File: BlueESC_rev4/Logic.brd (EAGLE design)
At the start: 24.4 x 36 mm, 37 parts, among them U1 ATMEGA168, U2 V_REG_LDOSMD, Y1 RESONATORSMD

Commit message: Commit before major changes to rev 4
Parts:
- R15: value 22 -> 150
- R16: value 22 -> 100
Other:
- board text added: "BLUESC-ELEC-LOGIC-X1B"
- board text removed: "BLUESC-ELEC-LOGIC-X1A"
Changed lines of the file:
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@@
 <hole x="23.495" y="10.795" drill="2.8"/>
 <hole x="27.305" y="10.795" drill="2.8"/>
-<text x="31.115" y="43.02125" size="0.6096" layer="51" rot="R180">BLUESC-ELEC-LOGIC-X1A</text>
+<text x="31.115" y="43.02125" size="0.6096" layer="51" rot="R180">BLUESC-ELEC-LOGIC-X1B</text>
 <text x="23.495" y="20.6375" size="0.6096" layer="51" rot="R180">GND</text>
 <text x="25.0825" y="20.6375" size="0.6096" layer="51" rot="R180">5V</text>
@@
 <element name="R13" library="SparkFun-Resistors" package="0603-RES" value="10K" x="23.92375" y="14.57" rot="R270"/>
 <element name="R14" library="SparkFun-Resistors" package="0603-RES" value="10K" x="26.46375" y="14.605" rot="R270"/>
-<element name="R15" library="SparkFun" package="0603-RES" value="22" x="21.55" y="14.56" rot="R90"/>
-<element name="R16" library="SparkFun" package="0603-RES" value="22" x="28.94" y="14.5575" rot="R90"/>
+<element name="R15" library="SparkFun" package="0603-RES" value="150" x="21.55" y="14.56" rot="R90"/>
+<element name="R16" library="SparkFun" package="0603-RES" value="100" x="28.94" y="14.5575" rot="R90"/>
 <element name="R2" library="SparkFun-Resistors" package="0603-RES" value="47K" x="20.0025" y="26.19375" rot="R180"/>
 <element name="R3" library="SparkFun-Resistors" package="0603-RES" value="47K" x="19.52625" y="28.8925" rot="R90"/>

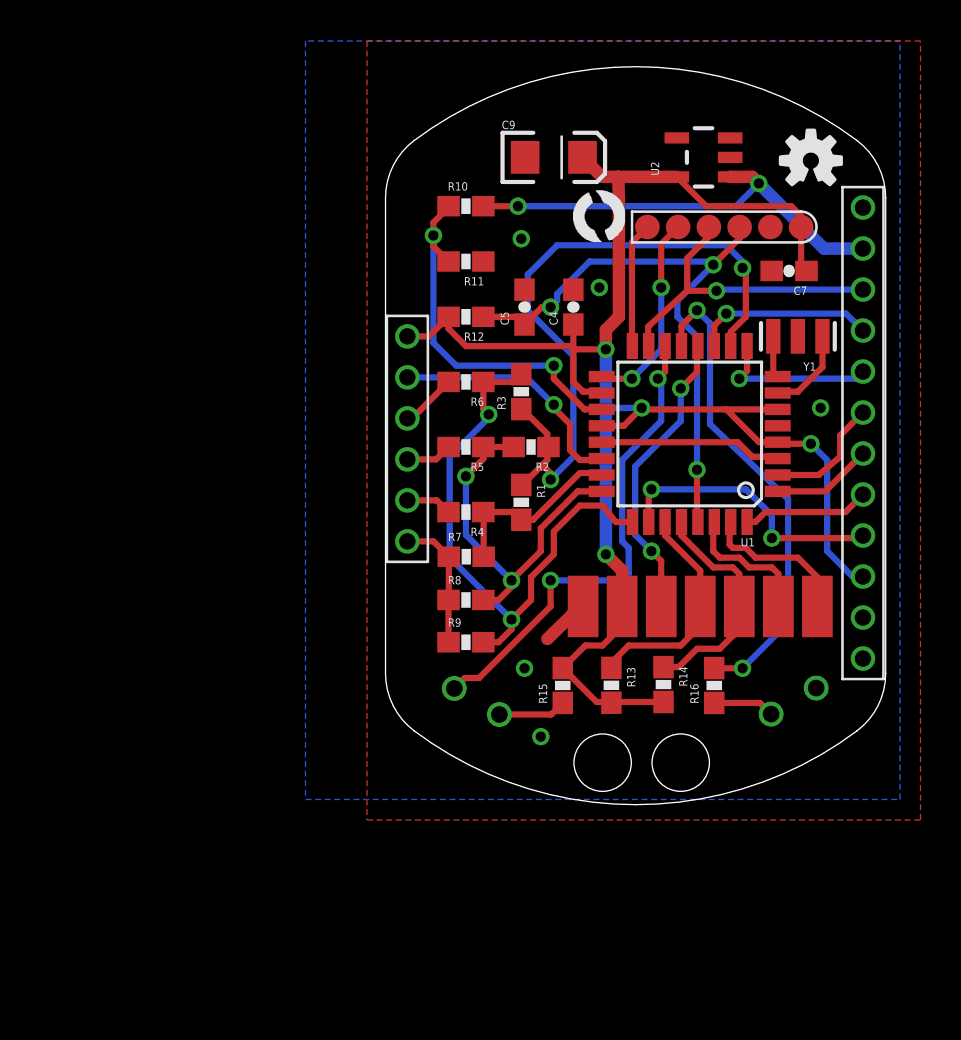
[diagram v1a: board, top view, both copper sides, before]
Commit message: Major updates on revision 4 include rearranged components, removal of programming pins, and new board shapes.
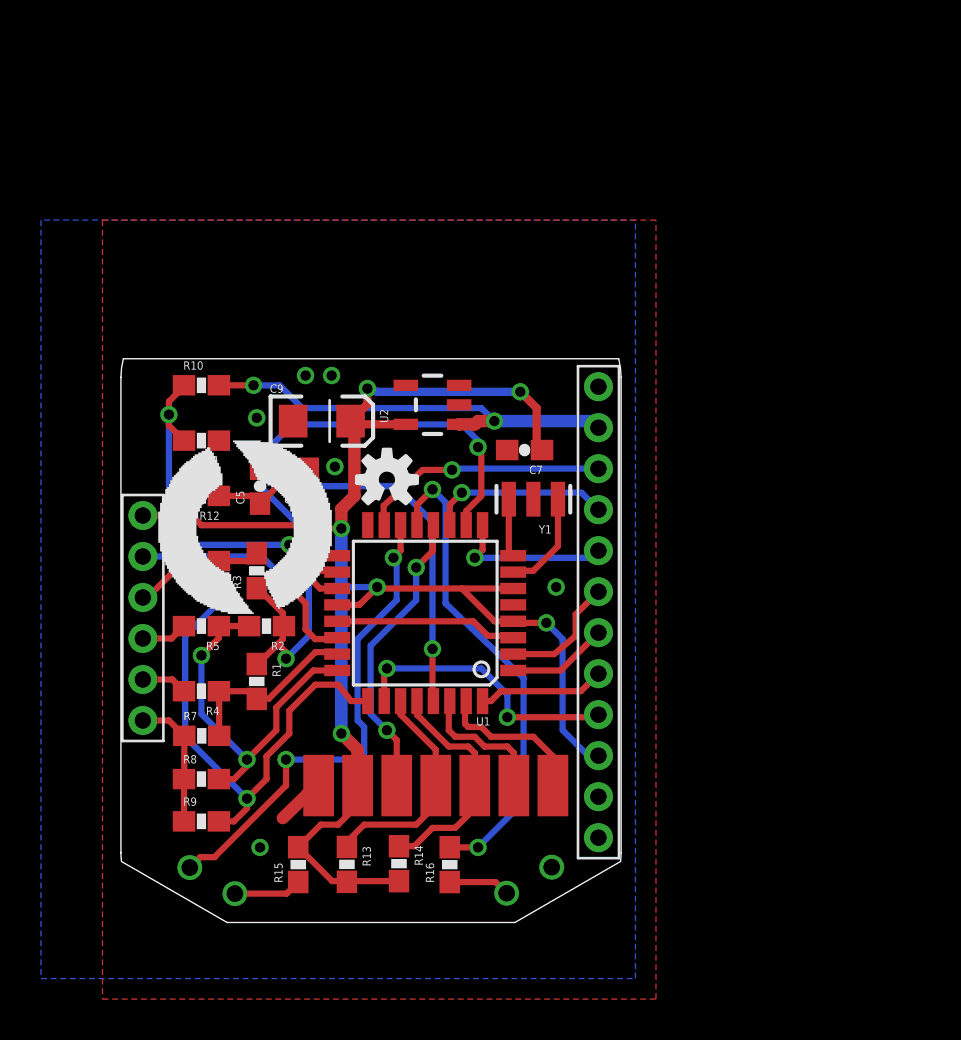
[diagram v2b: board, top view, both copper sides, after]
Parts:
- removed U$14: AVR-ISPTINY-SMD, BR-Eagle-Library:AVR-ISP-TINY
- U$4: value LOGOBR-LOGO-S -> LOGOBR-LOGO-M; device BR-Eagle-Library:BR-LOGO-SMALL -> BR-Eagle-Library:BR-LOGO-MEDIUM
- moved U$4 27.1 mm to (1.86, 18.1)
- moved LOGO1 25.9 mm to (13.0, 24.6)
- moved U2 17.9 mm to (15.2, 28.3)
- moved C9 17.1 mm to (9.80, 27.5)
- moved C4 15.6 mm to (9.16, 24.3)
- moved R12 15.6 mm to (3.92, 23.8)
- moved R8 15.6 mm to (3.92, 9.99)
- moved C5 15.6 mm to (6.78, 24.3)
- moved C7 15.6 mm to (19.7, 26.0)
- moved LED1 15.6 mm to (19.9, 5.06)
- moved R1 15.6 mm to (6.62, 14.8)
- moved R13 15.6 mm to (11.0, 5.83)
- moved R14 15.6 mm to (13.6, 5.87)
- moved R16 15.6 mm to (16.0, 5.82)
- moved R2 15.6 mm to (7.10, 17.5)
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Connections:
- net GND: no longer U$14.GND
- net MISO: no longer U$14.MISO
- net PWM_CL: no longer U$14.MOSI
- net RESET: no longer U$14.RESET
- net SCK: no longer U$14.SCK
- net VCC5V: no longer U$14.VCC
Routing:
- net SCK: track 9.85 -> 0.00 mm, vias 2 -> 0
- net RESET: track 29.1 -> 20.5 mm, vias 3 -> 2
- net MISO: track 6.12 -> 0.03 mm
- net PWM_CL: track 15.7 -> 12.1 mm
- net VCC5V: track 85.8 -> 83.5 mm, vias 4 -> 6
- net N$10: track 4.21 -> 5.00 mm
- net N$11: track 2.05 -> 2.85 mm
- net VBAT: track 21.8 -> 21.2 mm
- net GND: vias 5 -> 6
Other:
- board size 24.4 x 36 mm -> 24.4 x 27.5 mm
- board text added: "1/15"
- board text added: "B"
- board text added: "R"
- board text added: "rev4"
- board text removed: "+"
- board text removed: "-"
- board text removed: "9/14"
- board text removed: "Blue"
- board text removed: "Robotics"

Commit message: Minor changes before ordering production boards.
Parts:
- R15: value 150 -> 2.2K
- R16: value 100 -> 150
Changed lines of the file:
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@@
 <element name="R13" library="SparkFun-Resistors" package="0603-RES" value="10K" x="11.02055" y="5.8324" rot="R270"/>
 <element name="R14" library="SparkFun-Resistors" package="0603-RES" value="10K" x="13.56055" y="5.8674" rot="R270"/>
-<element name="R15" library="SparkFun" package="0603-RES" value="150" x="8.6468" y="5.8224" rot="R90"/>
-<element name="R16" library="SparkFun" package="0603-RES" value="100" x="16.0368" y="5.8199" rot="R90"/>
+<element name="R15" library="SparkFun" package="0603-RES" value="2.2K" x="8.6468" y="5.8224" rot="R90"/>
+<element name="R16" library="SparkFun" package="0603-RES" value="150" x="16.0368" y="5.8199" rot="R90"/>
 <element name="R2" library="SparkFun-Resistors" package="0603-RES" value="47K" x="7.0993" y="17.45615" rot="R180"/>
 <element name="R3" library="SparkFun-Resistors" package="0603-RES" value="47K" x="6.62305" y="20.1549" rot="R90"/>
